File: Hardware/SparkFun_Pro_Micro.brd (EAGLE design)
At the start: 17.8 x 33 mm, 105 parts, among them J2 Qwiic, U1 3.3V, U3 ATmega32U4, Y2 16MHz

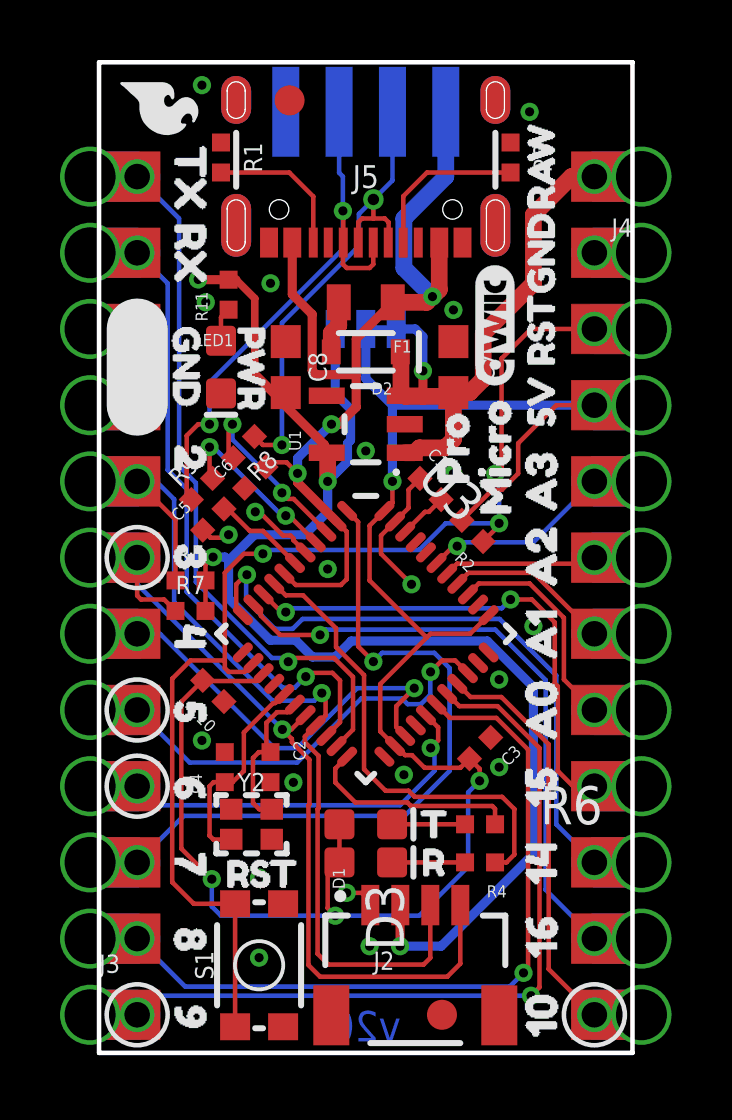
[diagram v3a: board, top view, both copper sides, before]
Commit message: Correct prodID on 22 ohm resistors.
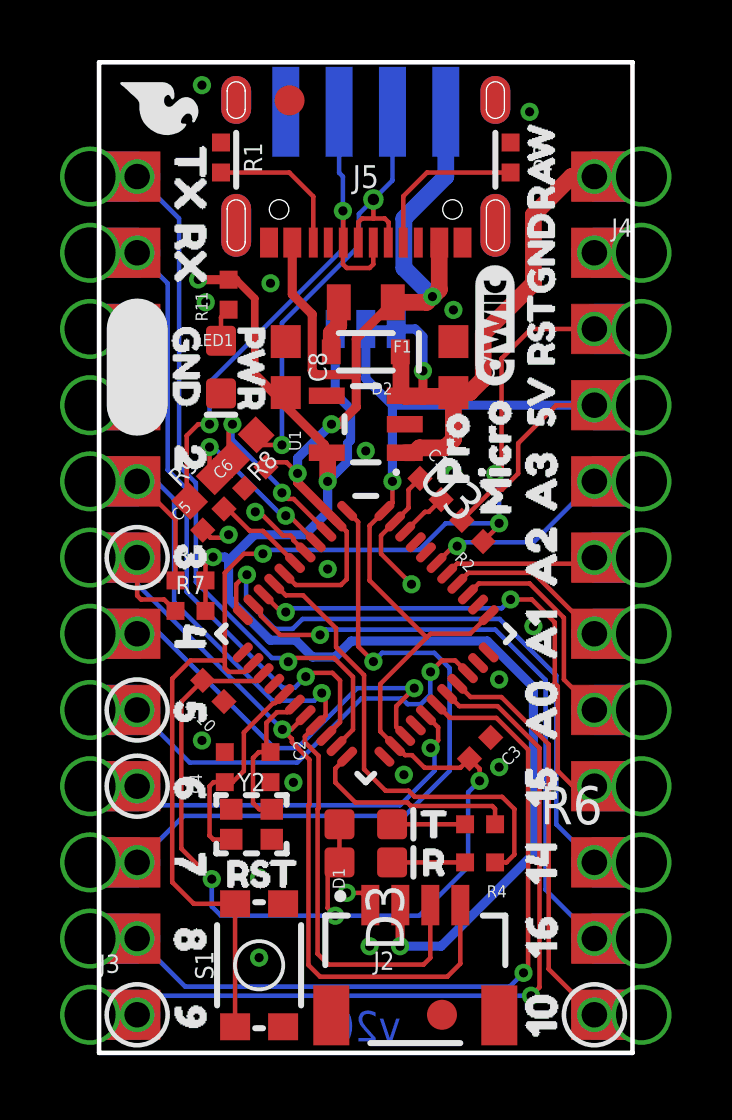
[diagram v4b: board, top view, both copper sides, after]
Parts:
- R8, R9: device SparkFun-Resistors:0402-TIGHT -> SparkFun-Resistors:0402
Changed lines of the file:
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@@
 <attribute name="VALUE" x="8.89" y="1.624" size="0.6096" layer="27" font="vector" ratio="20"/>
 </element>
-<element name="R8" library="SparkFun-Resistors" package="0402-TIGHT" value="22" x="4.826" y="20.193" smashed="yes" rot="R225">
+<element name="R8" library="SparkFun-Resistors" package="0402" value="22" x="4.826" y="20.193" smashed="yes" rot="R225">
 <attribute name="NAME" x="5.223396875" y="19.79560625" size="0.6096" layer="25" font="vector" ratio="20" rot="R225" align="bottom-center"/>
-<attribute name="PROD_ID" value="RES-14340" x="4.826" y="20.193" size="1.778" layer="27" font="vector" ratio="15" rot="R225" display="off"/>
-<attribute name="VALUE" x="4.42860625" y="20.590396875" size="0.6096" layer="27" font="vector" ratio="20" rot="R225" align="top-center"/>
-</element>
-<element name="R9" library="SparkFun-Resistors" package="0402-TIGHT" value="22" x="3.429" y="18.796" smashed="yes" rot="R45">
+<attribute name="PROD_ID" value="RES-12427" x="4.826" y="20.193" size="1.778" layer="27" font="vector" ratio="15" rot="R225" display="off"/>
+<attribute name="VALUE" value="22" x="4.42860625" y="20.590396875" size="0.6096" layer="27" font="vector" ratio="20" rot="R225" align="top-center"/>
+</element>
+<element name="R9" library="SparkFun-Resistors" package="0402" value="22" x="3.429" y="18.796" smashed="yes" rot="R45">
 <attribute name="NAME" x="3.031603125" y="19.19339375" size="0.6096" layer="25" font="vector" ratio="20" rot="R45" align="bottom-center"/>
-<attribute name="PROD_ID" value="RES-14340" x="3.429" y="18.796" size="1.778" layer="27" font="vector" ratio="15" rot="R45" display="off"/>
-<attribute name="VALUE" x="3.82639375" y="18.398603125" size="0.6096" layer="27" font="vector" ratio="20" rot="R45" align="top-center"/>
+<attribute name="PROD_ID" value="RES-12427" x="3.429" y="18.796" size="1.778" layer="27" font="vector" ratio="15" rot="R45" display="off"/>
+<attribute name="VALUE" value="22" x="3.82639375" y="18.398603125" size="0.6096" layer="27" font="vector" ratio="20" rot="R45" align="top-center"/>
 </element>
 <element name="U$13" library="buzzard_labels (13)" package="45" value="" x="3.048" y="15.367" smashed="yes" rot="R270"/>
@@
 <wire x1="4.445" y1="20.955" x2="4.318" y2="20.828" width="0.1524" layer="1"/>
 <wire x1="4.318" y1="20.828" x2="4.318" y2="19.9938875" width="0.1524" layer="1"/>
-<wire x1="4.47244375" y1="19.83944375" x2="4.318" y2="19.9938875" width="0.1524" layer="1"/>
+<wire x1="4.415875" y1="19.782875" x2="4.318" y2="19.9938875" width="0.1524" layer="1"/>
 </signal>
 <signal name="D+">
@@
 <via x="3.683" y="20.193" extent="1-16" drill="0.3048"/>
 <wire x1="7.2229" y1="17.021421875" x2="6.337321875" y2="17.907" width="0.1524" layer="1"/>
-<wire x1="3.782553125" y1="19.149553125" x2="3.683" y2="19.24910625" width="0.1524" layer="1"/>
+<wire x1="3.839121875" y1="19.206121875" x2="3.683" y2="19.24910625" width="0.1524" layer="1"/>
 <wire x1="3.683" y1="19.24910625" x2="3.683" y2="20.193" width="0.1524" layer="1"/>
 </signal>
@@
 <wire x1="6.096" y1="24.33394375" x2="6.096" y2="20.2638" width="0.1524" layer="16"/>
 <via x="6.096" y="20.2638" extent="1-16" drill="0.3048"/>
-<wire x1="5.179553125" y1="20.546553125" x2="5.46230625" y2="20.2638" width="0.1524" layer="1"/>
+<wire x1="5.236121875" y1="20.603121875" x2="5.46230625" y2="20.2638" width="0.1524" layer="1"/>
 <wire x1="5.46230625" y1="20.2638" x2="6.096" y2="20.2638" width="0.1524" layer="1"/>
 <contactref element="JP14" pad="D-"/>
@@
 <wire x1="3.302" y1="20.955" x2="2.921" y2="20.574" width="0.1524" layer="1"/>
 <wire x1="2.921" y1="20.574" x2="2.921" y2="18.5968875" width="0.1524" layer="1"/>
-<wire x1="3.07544375" y1="18.44244375" x2="2.921" y2="18.5968875" width="0.1524" layer="1"/>
+<wire x1="3.018875" y1="18.385875" x2="2.921" y2="18.5968875" width="0.1524" layer="1"/>
 <via x="3.683" y="20.955" extent="1-16" drill="0.3048"/>
 <contactref element="JP14" pad="D+"/>

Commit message: Update SparkFun_Pro_Micro.brd
- Adding board dimensions
- Add additional distance between connectors to edge of board
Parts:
- moved FRAME1 14.0 mm to (20.3, -22.9)
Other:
- board text added: "Units in Inches"
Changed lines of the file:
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@@
 <?xml version="1.0" encoding="utf-8"?>
 <!DOCTYPE eagle SYSTEM "eagle.dtd">
-<eagle version="9.5.2">
+<eagle version="9.5.0">
 <drawing>
 <settings>
-<setting alwaysvectorfont="yes"/>
+<setting alwaysvectorfont="no"/>
 <setting keepoldvectorfont="yes"/>
 <setting verticaltext="up"/>
@@
 <layer number="45" name="Holes" color="7" fill="1" visible="yes" active="yes"/>
 <layer number="46" name="Milling" color="3" fill="1" visible="no" active="yes"/>
-<layer number="47" name="Measures" color="7" fill="1" visible="no" active="yes"/>
+<layer number="47" name="Measures" color="7" fill="1" visible="yes" active="yes"/>
 <layer number="48" name="Document" color="7" fill="1" visible="no" active="yes"/>
 <layer number="49" name="Reference" color="13" fill="1" visible="no" active="yes"/>
@@
 <wire x1="8.89" y1="9.017" x2="13.843" y2="13.97" width="0.0508" layer="49"/>
 <wire x1="13.843" y1="13.97" x2="8.89" y2="18.923" width="0.0508" layer="49"/>
-<text x="51.435" y="-9.144" size="1.778" layer="51" font="vector" ratio="15">N Seidle</text>
+<text x="51.435" y="-23.114" size="1.778" layer="51" font="vector" ratio="15">N Seidle</text>
 <text x="26.67" y="36.83" size="2.54" layer="51" font="vector" ratio="15">0.8mm PCB</text>
+<dimension x1="0" y1="0" x2="0" y2="33.02" x3="-3.81" y3="16.51" textsize="1.778" textratio="15" layer="47" unit="inch"/>
+<dimension x1="1.27" y1="29.21" x2="0" y2="29.21" x3="0.635" y3="36.83" textsize="1.778" textratio="15" layer="47" unit="inch"/>
+<dimension x1="0" y1="33.02" x2="8.89" y2="33.02" x3="4.445" y3="41.91" textsize="1.778" textratio="15" layer="47" unit="inch"/>
+<dimension x1="10.541" y1="4.926" x2="0" y2="4.926" x3="5.2705" y3="-3.77126875" textsize="1.778" textratio="15" layer="47" unit="inch"/>
+<dimension x1="0" y1="0" x2="17.78" y2="0" x3="8.89" y3="-8.89" textsize="1.778" textratio="15" layer="47" unit="inch"/>
+<text x="-2.54" y="-13.97" size="1.778" layer="47" font="vector" ratio="15">Units in Inches</text>
 </plain>
 <attributes>
@@
 <element name="U$65" library="buzzard_labels (10)" package="5V1" value="" x="14.732" y="20.066" smashed="yes" rot="R90"/>
 <element name="U$15" library="buzzard_labels (10)" package="5V1" value="" x="16.383" y="21.59" smashed="yes" rot="MR0"/>
-<element name="FRAME1" library="SparkFun-Aesthetics" package="CREATIVE_COMMONS" value="FRAME-LETTER" x="20.32" y="-8.89" smashed="yes">
-<attribute name="DESIGNER" value="" x="20.32" y="-8.89" size="1.778" layer="27" font="vector" ratio="15" display="off"/>
-<attribute name="REV" value="" x="20.32" y="-8.89" size="1.778" layer="27" font="vector" ratio="15" display="off"/>
+<element name="FRAME1" library="SparkFun-Aesthetics" package="CREATIVE_COMMONS" value="FRAME-LETTER" x="20.32" y="-22.86" smashed="yes">
+<attribute name="DESIGNER" value="" x="20.32" y="-22.86" size="1.778" layer="27" font="vector" ratio="15" display="off"/>
+<attribute name="REV" value="" x="20.32" y="-22.86" size="1.778" layer="27" font="vector" ratio="15" display="off"/>
 </element>
 <element name="LOGO5" library="SparkFun-Aesthetics" package="ORDERING_INSTRUCTIONS" value="SPECIAL_INSTRUCTIONS-ORDERING" x="22.86" y="50.8" smashed="yes"/>
